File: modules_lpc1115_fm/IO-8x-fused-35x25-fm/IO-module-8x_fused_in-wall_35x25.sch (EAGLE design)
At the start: 75 parts, among them IC1 LPC1115, IC2 ATAES132A-SHEQ-T, Q2 ASFL, U1 EEPROM, X3 MICROMATCH-10

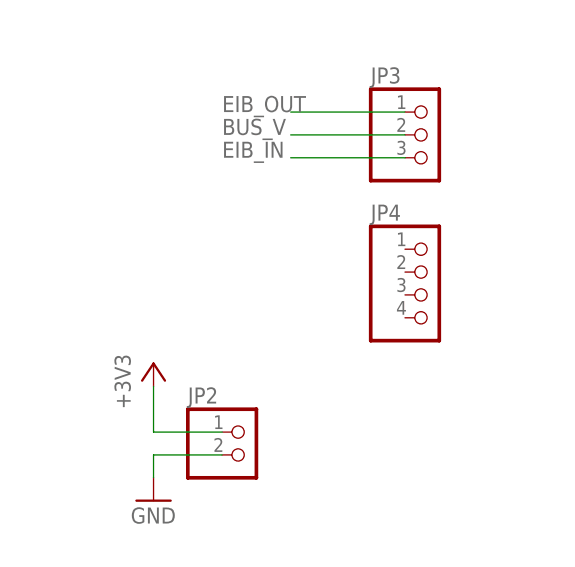
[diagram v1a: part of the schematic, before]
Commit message: [IOmodule8xUP]  added holes / change BB-fixing-pins from 4 to 2
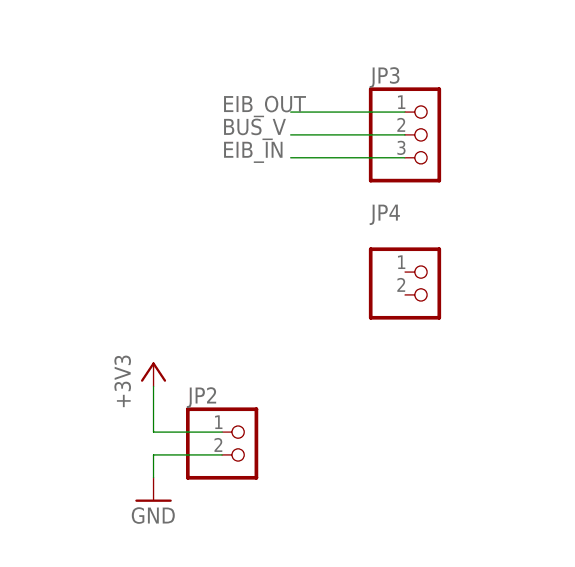
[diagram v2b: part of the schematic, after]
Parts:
- JP4: device pinhead_dmx:PINHD-1X4 -> pinhead_dmx:PINHD-1X2
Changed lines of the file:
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@@
 <part name="FB10" library="microbuilder" deviceset="FERRITE" device="0805"/>
 <part name="JP2" library="pinhead_dmx" deviceset="PINHD-1X2" device="" package3d_urn="urn:adsk.eagle:package:22435/2"/>
-<part name="JP4" library="pinhead_dmx" deviceset="PINHD-1X4" device="" package3d_urn="urn:adsk.eagle:package:22407/2"/>
+<part name="JP4" library="pinhead_dmx" deviceset="PINHD-1X2" device="" package3d_urn="urn:adsk.eagle:package:22435/2"/>
 <part name="LED3" library="led" library_urn="urn:adsk.eagle:library:259" deviceset="LED" device="CHIPLED_1206" package3d_urn="urn:adsk.eagle:package:15823/2" value="red SMD">
 <attribute name="REICHELT" value="SMD-LED 0805 RT"/>
@@
 <attribute name="VALUE" x="481.33" y="144.78" size="1.778" layer="96"/>
 </instance>
-<instance part="JP4" gate="A" x="508" y="167.64" smashed="yes">
+<instance part="JP4" gate="G$1" x="508" y="167.64" smashed="yes">
 <attribute name="NAME" x="501.65" y="175.895" size="1.778" layer="95"/>
 <attribute name="VALUE" x="501.65" y="160.02" size="1.778" layer="96"/>

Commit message: [IOmodule8xUP] added JST ZH connector for I2C; reordered
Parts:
- removed R26: 100k, rcl:R-EU_R0805
- removed R27: 0R, rcl:R-EU_R0805
- added JP1: B4B-ZR, jst:B4B-ZR
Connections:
- removed net N$11: Q2.OE, R26.1, R27.2
- net +3V3: now also JP1.2, Q2.OE, X3-2.S; no longer R26.2, X3-1.S
- net GND: now also JP1.1, X3-1.S; no longer X3-2.S
- net ISP_EN: now also TVS3.IO3; no longer TVS3.IO4
- net RESET: now also TVS3.IO4; no longer TVS3.IO3
- net SCL: now also JP1.4
- net SDA: now also JP1.3
- net XTAL_EN: no longer R27.1
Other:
- moved on the sheet: JP4, X3-1, X3-10, X3-2, X3-3, X3-4, X3-5, X3-6, X3-7, X3-8, X3-9

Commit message: [IOmodule8xUP] massive re-arrangement
divided part so that 4 IOs are on TOP and 4 IOs on BOT
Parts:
- JP1: value B4B-ZR -> B5B-ZR; device jst:B4B-ZR -> jst:B5B-ZR
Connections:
- removed net IO114: IC1.PIO0_2/SSEL0/CT16B0_CAP0
- removed net N$14: F21.2, R44.1, TVS8.IO1
- removed net N$20: F22.2, R45.1, TVS8.IO4
- new net N$11: F18.2, R41.1, TVS7.IO1
- new net N$12: F17.2, R40.1, TVS7.IO4
- net IN6: now also X3-9.S; no longer X3-8.S
- net IN7: now also X3-8.S; no longer X3-9.S
- net IO1: now also D40.A2, IC1.PIO3_4/CT16B0_CAP1/RXD; no longer D40.A1, IC1.PIO2_1/DSR/SCK1
- net IO2: now also D40.A1; no longer D40.A2
- net IO6: now also IC1.PIO2_1/DSR/SCK1; no longer IC1.PIO2_10
- net N$13: now also TVS8.IO4; no longer TVS8.IO2
- net N$16: now also F24.2, R47.1, TVS8.IO1; no longer F18.2, R41.1, TVS7.IO4
- net N$18: now also F21.2, R44.1, TVS8.IO3; no longer F17.2, R40.1, TVS7.IO1
- net N$9: now also F22.2, R45.1, TVS8.IO2; no longer F24.2, R47.1, TVS8.IO3
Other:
- moved on the sheet: C15, C9, D40, IC2, JP2, JP3, JP4, JP8, LED1, LED2, LED3, R1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

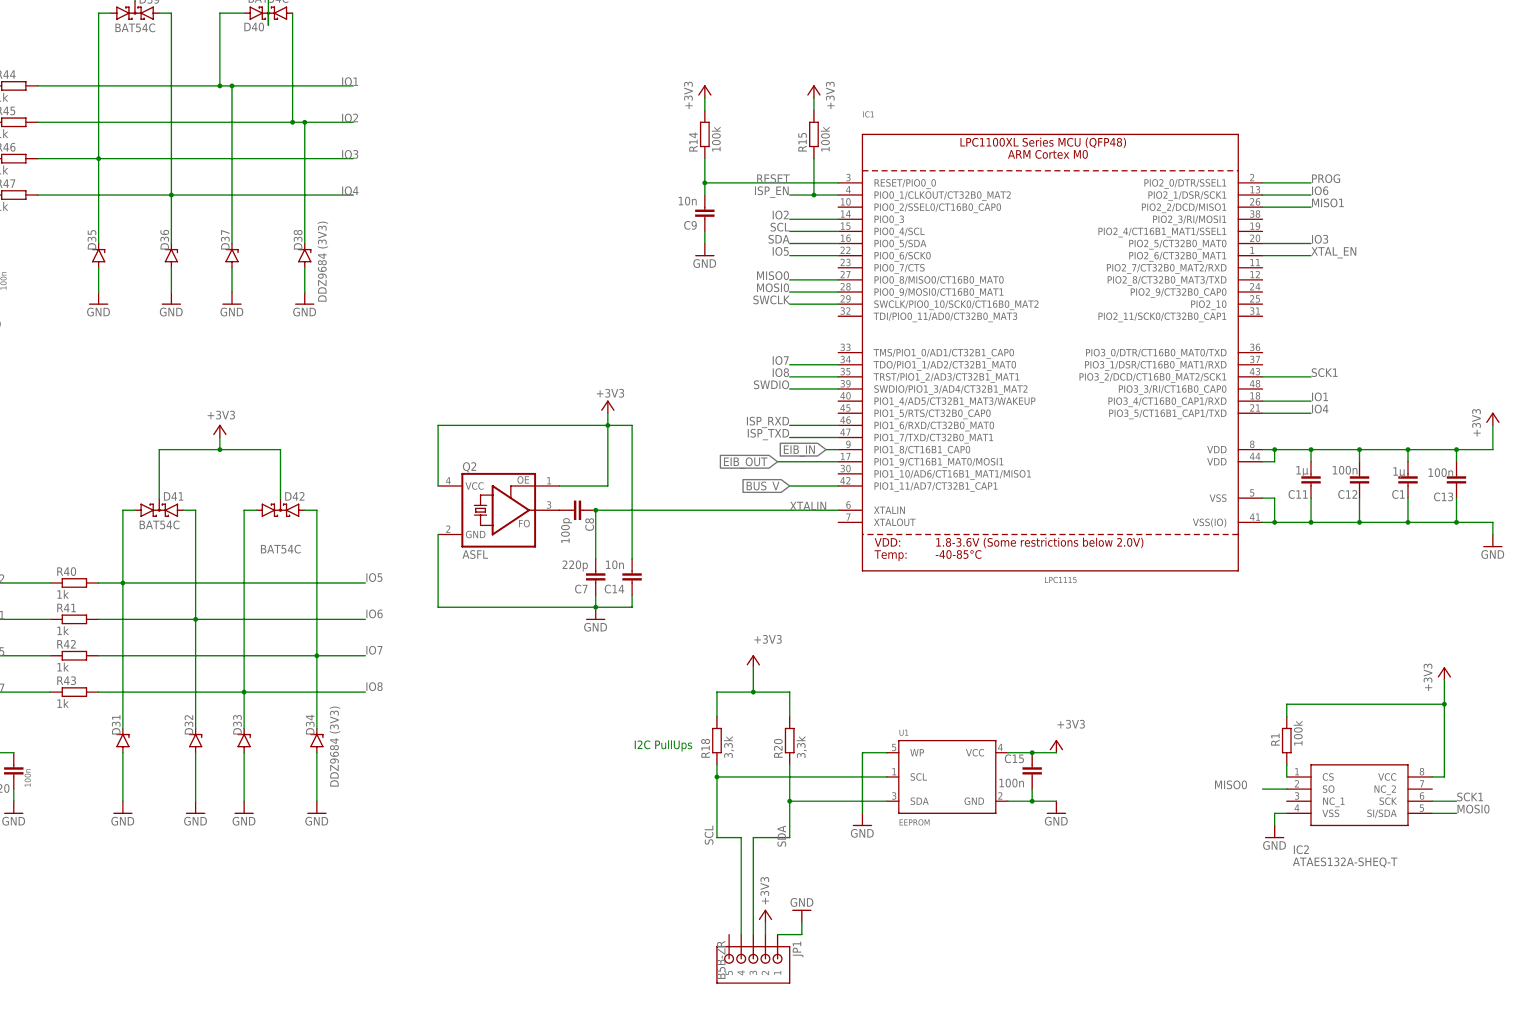
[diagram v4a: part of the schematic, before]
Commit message: [IOmodule8xUP]  optimized names & values positions; changed JP1 to 2mm
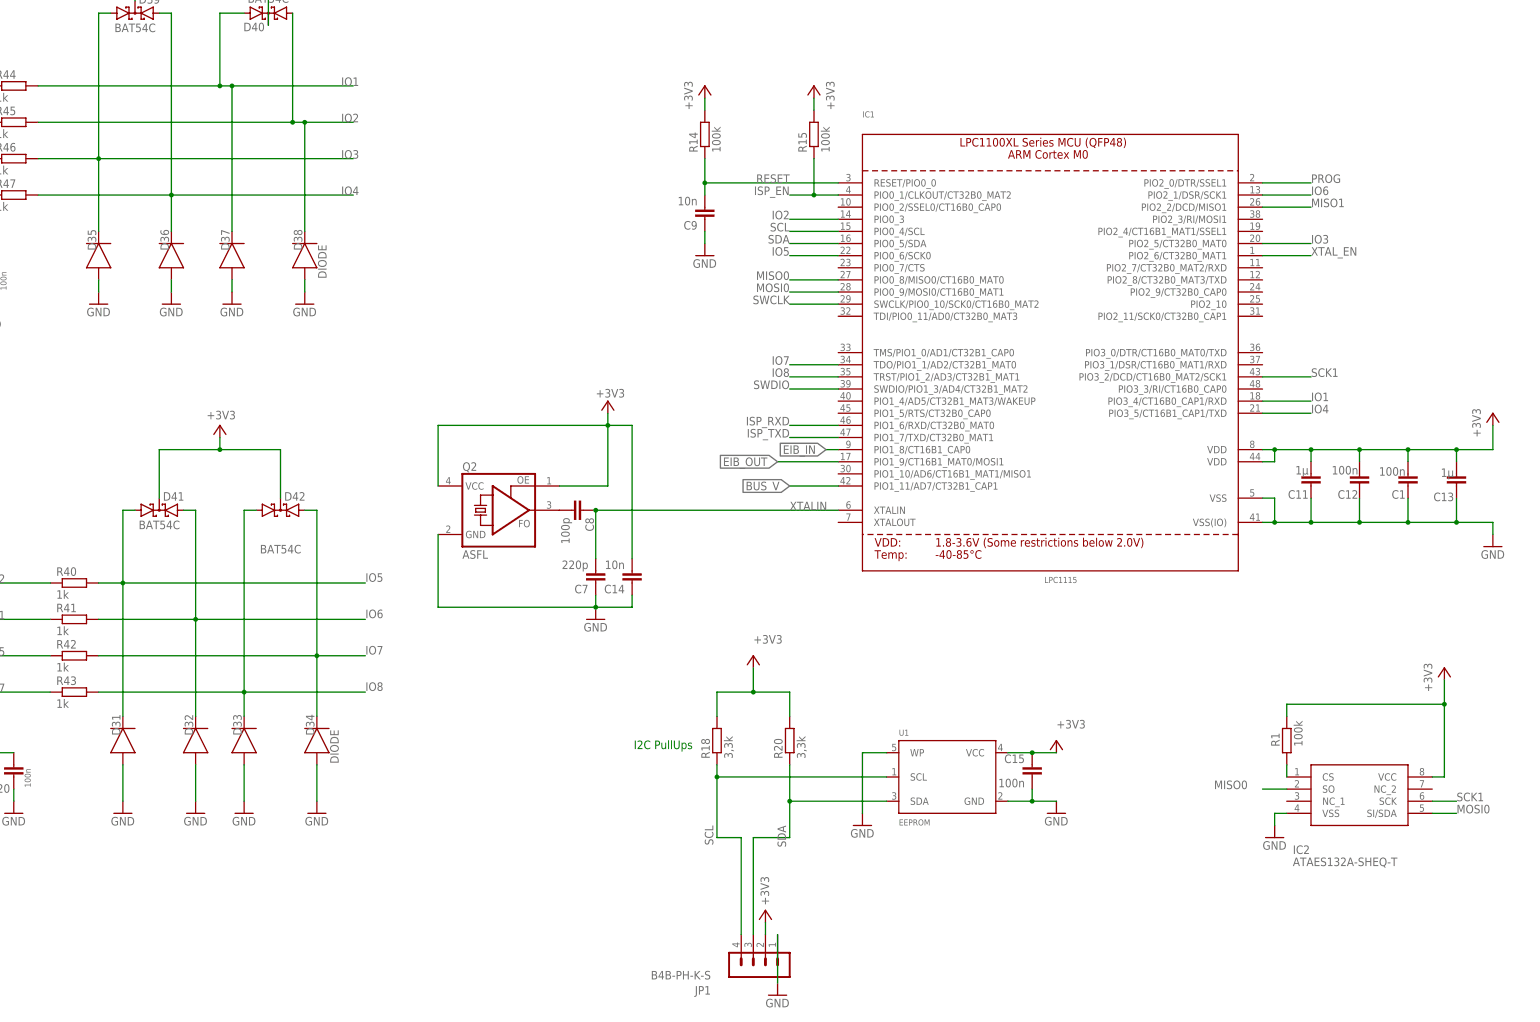
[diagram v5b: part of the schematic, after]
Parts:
- C1: value 1µ -> 100n
- C13: value 100n -> 1µ
- D31, D32, D33, D34, D35, D36, D37, D38: value DDZ9684 (3V3) -> DIODE; device Diode:ZENER_MMSZ5240BTDO-219-AB(SOD123F) -> Diode:DIODE_DO-219-AB(SOD123F)
- JP1: value B5B-ZR -> B4B-PH-K-S; device jst:B5B-ZR -> con-JST PH:B4B-PH-K-S

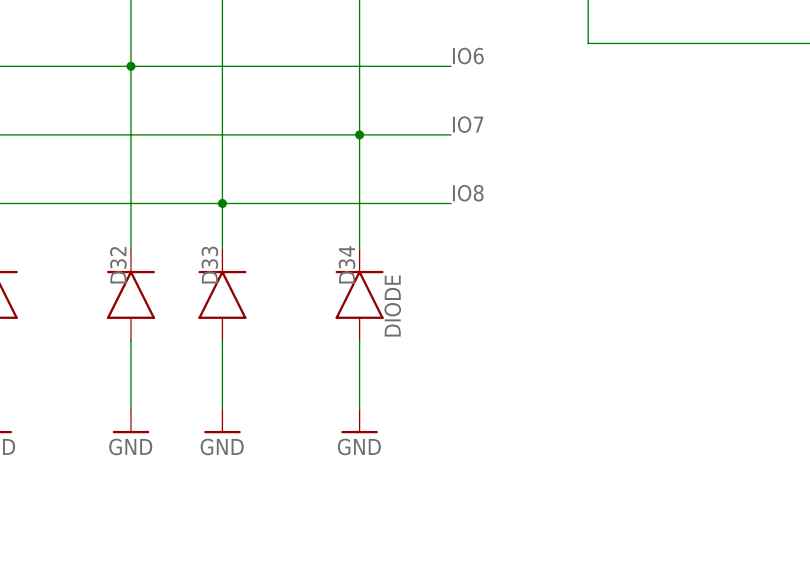
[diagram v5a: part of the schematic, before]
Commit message: [IOmodule8xUP] vias added, Z-Diode Value changed
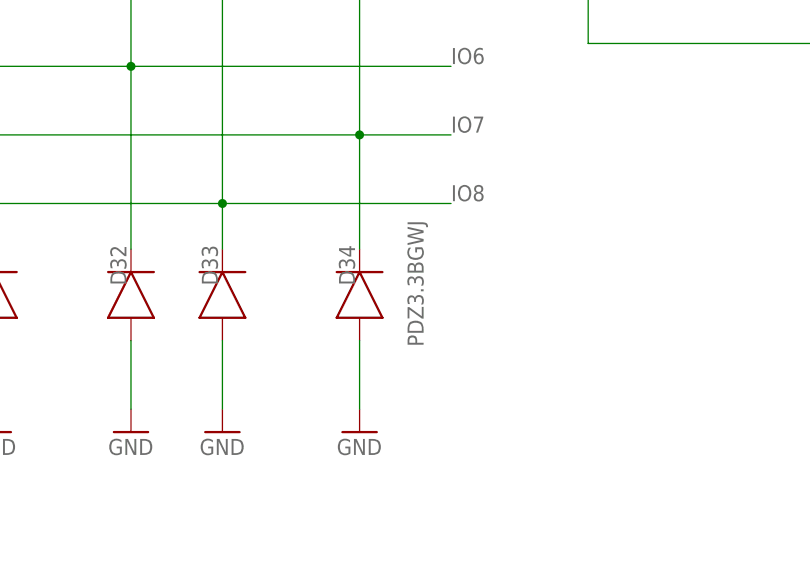
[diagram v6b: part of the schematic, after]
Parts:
- D31: value DIODE -> DDZ9684
- D34: value DIODE -> PDZ3.3BGWJ
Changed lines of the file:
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@@
 <part name="GND51" library="supply1" library_urn="urn:adsk.eagle:library:371" deviceset="GND" device=""/>
 <part name="GND52" library="supply1" library_urn="urn:adsk.eagle:library:371" deviceset="GND" device=""/>
-<part name="D31" library="Diode" deviceset="DIODE" device="DO-219-AB(SOD123F)" package3d_urn="urn:adsk.eagle:package:9427153/2" technology="_" value="DIODE"/>
+<part name="D31" library="Diode" deviceset="DIODE" device="DO-219-AB(SOD123F)" package3d_urn="urn:adsk.eagle:package:9427153/2" technology="_" value="DDZ9684"/>
 <part name="D32" library="Diode" deviceset="DIODE" device="DO-219-AB(SOD123F)" package3d_urn="urn:adsk.eagle:package:9427153/2" technology="_" value="DIODE"/>
 <part name="D33" library="Diode" deviceset="DIODE" device="DO-219-AB(SOD123F)" package3d_urn="urn:adsk.eagle:package:9427153/2" technology="_" value="DIODE"/>
-<part name="D34" library="Diode" deviceset="DIODE" device="DO-219-AB(SOD123F)" package3d_urn="urn:adsk.eagle:package:9427153/2" technology="_" value="DIODE"/>
+<part name="D34" library="Diode" deviceset="DIODE" device="DO-219-AB(SOD123F)" package3d_urn="urn:adsk.eagle:package:9427153/2" technology="_" value="PDZ3.3BGWJ"/>
 <part name="TVS8" library="usblc6" deviceset="USBLC6-4" device="SC6" package3d_urn="urn:adsk.eagle:package:25303836/1"/>
 <part name="C21" library="rcl" library_urn="urn:adsk.eagle:library:334" deviceset="C-EU" device="C0805" package3d_urn="urn:adsk.eagle:package:23617/2" value="100n"/>
@@
 <instance part="D34" gate="G$1" x="167.64" y="33.02" smashed="yes" rot="R90">
 <attribute name="NAME" x="166.243" y="36.322" size="1.778" layer="95" rot="R90" align="center"/>
-<attribute name="VALUE" x="171.323" y="31.75" size="1.778" layer="96" rot="R90" align="center"/>
+<attribute name="VALUE" x="173.863" y="34.29" size="1.778" layer="96" rot="R90" align="center"/>
 </instance>
 <instance part="TVS8" gate="G$1" x="73.66" y="134.62" smashed="yes">

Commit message: [IOmodule8xUP] added 100R resistor to each IO
Protection of potential mess with 3V3 Z-Diodes when ARM pins run in high mode
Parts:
- added R2, R3, R4, R5, R6, R7, R8, R9: 1k, rcl:R-EU_R0805
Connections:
- new net IO1B: D37.C, D40.A2, R44.2, R9.1
- new net IO2B: D38.C, D40.A1, R3.1, R45.2
- new net IO3B: D35.C, D39.A1, R46.2, R7.1
- new net IO4B: D36.C, D39.A2, R47.2, R8.1
- new net IO5B: D31.C, D41.A1, R40.2, R6.1
- new net IO6B: D32.C, D41.A2, R2.1, R41.2
- new net IO7B: D34.C, D42.A2, R4.1, R42.2
- new net IO8B: D33.C, D42.A1, R43.2, R5.1
- net IO1: now also R9.2; no longer D37.C, D40.A2, R44.2
- net IO2: now also R3.2; no longer D38.C, D40.A1, R45.2
- net IO3: now also R7.2; no longer D35.C, D39.A1, R46.2
- net IO4: now also R8.2; no longer D36.C, D39.A2, R47.2
- net IO5: now also R6.2; no longer D31.C, D41.A1, R40.2
- net IO6: now also R2.2; no longer D32.C, D41.A2, R41.2
- net IO7: now also R4.2; no longer D34.C, D42.A2, R42.2
- net IO8: now also R5.2; no longer D33.C, D42.A1, R43.2
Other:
- moved on the sheet: C1, C11, C12, C13, C14, C15, C20, C21, C7, C8, C9, D31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
